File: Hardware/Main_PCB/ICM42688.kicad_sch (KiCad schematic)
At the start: 6 parts, among them U1 ICM-42688-P

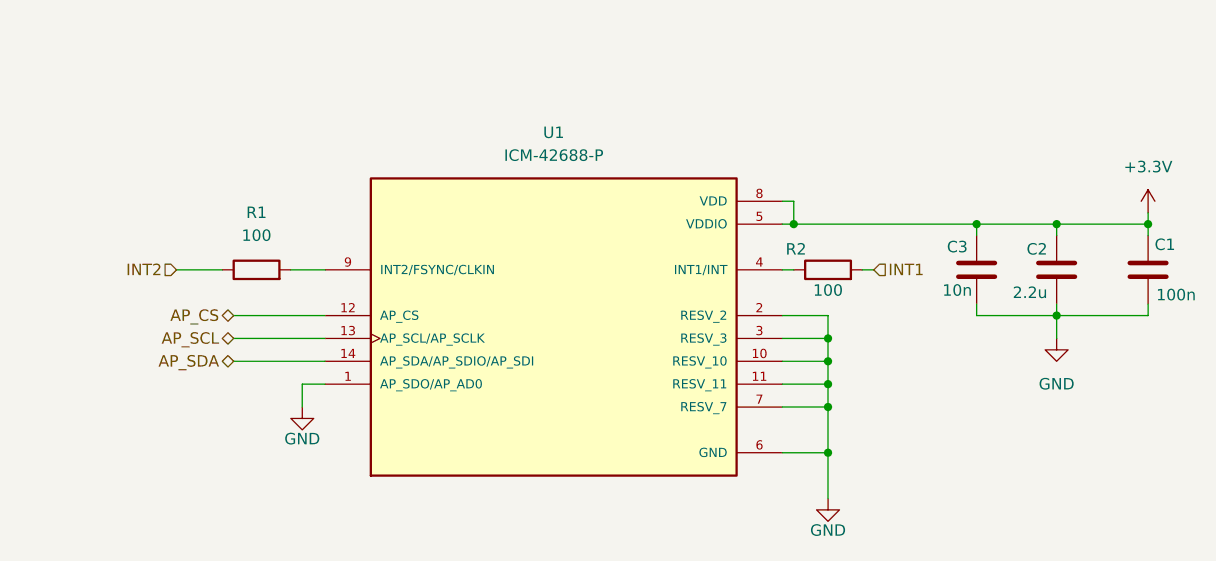
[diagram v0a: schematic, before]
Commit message: A finished version of the Main PCB schematic
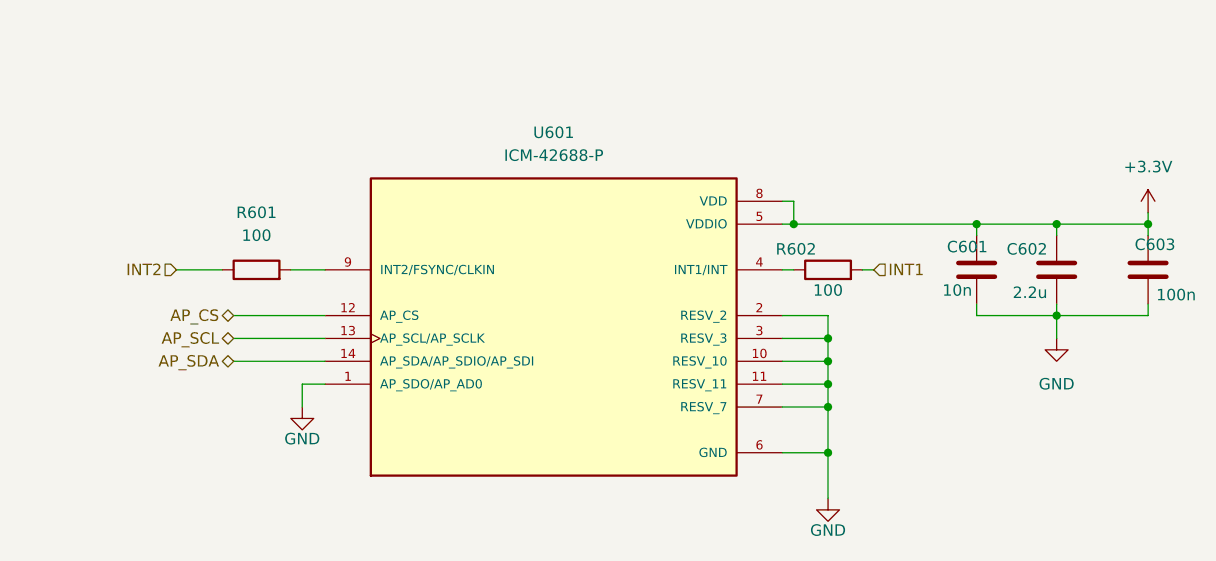
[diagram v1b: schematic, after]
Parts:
- renumbered C3 to C601, C2 to C602, C1 to C603, R1 to R601, R2 to R602, U1 to U601
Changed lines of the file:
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@@
 		(on_board yes)
 		(dnp no)
-		(property "Reference" "C3"
+		(property "Reference" "C601"
 			(at 136.398 54.61 0)
 			(effects
@@
 			(project "Main_PCB"
 				(path "/90d7beec-e1a2-46f8-bbb2-6b8f3489db10/c6d47e36-3031-4d07-ba70-df8c4b187df5"
-					(reference "C3")
+					(reference "C601")
 					(unit 1)
 				)
@@
 		(dnp no)
 		(fields_autoplaced yes)
-		(property "Reference" "R1"
+		(property "Reference" "R601"
 			(at 59.69 50.8 90)
 			(effects
@@
 			(project "Main_PCB"
 				(path "/90d7beec-e1a2-46f8-bbb2-6b8f3489db10/c6d47e36-3031-4d07-ba70-df8c4b187df5"
-					(reference "R1")
+					(reference "R601")
 					(unit 1)
 				)
@@
 		(on_board yes)
 		(dnp no)
-		(property "Reference" "C2"
+		(property "Reference" "C602"
 			(at 147.574 54.864 0)
 			(effects
@@
 			(project "Main_PCB"
 				(path "/90d7beec-e1a2-46f8-bbb2-6b8f3489db10/c6d47e36-3031-4d07-ba70-df8c4b187df5"
-					(reference "C2")
+					(reference "C602")
 					(unit 1)
 				)
@@
 		(on_board yes)
 		(dnp no)
-		(property "Reference" "R2"
+		(property "Reference" "R602"
 			(at 119.634 54.864 90)
 			(effects
@@
 			(project "Main_PCB"
 				(path "/90d7beec-e1a2-46f8-bbb2-6b8f3489db10/c6d47e36-3031-4d07-ba70-df8c4b187df5"
-					(reference "R2")
+					(reference "R602")
 					(unit 1)
 				)
@@
 		(dnp no)
 		(fields_autoplaced yes)
-		(property "Reference" "U1"
+		(property "Reference" "U601"
 			(at 92.71 41.91 0)
 			(effects
@@
 			(project "Main_PCB"
 				(path "/90d7beec-e1a2-46f8-bbb2-6b8f3489db10/c6d47e36-3031-4d07-ba70-df8c4b187df5"
-					(reference "U1")
+					(reference "U601")
 					(unit 1)
 				)
@@
 		(on_board yes)
 		(dnp no)
-		(property "Reference" "C1"
+		(property "Reference" "C603"
 			(at 161.798 54.356 0)
 			(effects
@@
 			(project "Main_PCB"
 				(path "/90d7beec-e1a2-46f8-bbb2-6b8f3489db10/c6d47e36-3031-4d07-ba70-df8c4b187df5"
-					(reference "C1")
+					(reference "C603")
 					(unit 1)
 				)
@@
 		(dnp no)
 		(fields_autoplaced yes)
-		(property "Reference" "#PWR019"
+		(property "Reference" "#PWR0604"
 			(at 158.75 54.61 0)
 			(effects
@@
 			(project "Main_PCB"
 				(path "/90d7beec-e1a2-46f8-bbb2-6b8f3489db10/c6d47e36-3031-4d07-ba70-df8c4b187df5"
-					(reference "#PWR019")
+					(reference "#PWR0604")
 					(unit 1)
 				)
@@
 		(on_board yes)
 		(dnp no)
-		(property "Reference" "#PWR022"
+		(property "Reference" "#PWR0601"
 			(at 64.77 78.74 0)
 			(effects
@@
 			(project "Main_PCB"
 				(path "/90d7beec-e1a2-46f8-bbb2-6b8f3489db10/c6d47e36-3031-4d07-ba70-df8c4b187df5"
-					(reference "#PWR022")
+					(reference "#PWR0601")
 					(unit 1)
 				)
@@
 		(on_board yes)
 		(dnp no)
-		(property "Reference" "#PWR024"
+		(property "Reference" "#PWR0602"
 			(at 123.19 88.9 0)
 			(effects
@@
 			(project "Main_PCB"
 				(path "/90d7beec-e1a2-46f8-bbb2-6b8f3489db10/c6d47e36-3031-4d07-ba70-df8c4b187df5"
-					(reference "#PWR024")
+					(reference "#PWR0602")
 					(unit 1)
 				)
@@
 		(dnp no)
 		(fields_autoplaced yes)
-		(property "Reference" "#PWR011"
+		(property "Reference" "#PWR0603"
 			(at 148.59 71.12 0)
 			(effects
@@
 			(project "Main_PCB"
 				(path "/90d7beec-e1a2-46f8-bbb2-6b8f3489db10/c6d47e36-3031-4d07-ba70-df8c4b187df5"
-					(reference "#PWR011")
-					(unit 1)
-				)
+					(reference "#PWR0603")
+					(unit 1)
+				)

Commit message: Added footprints to all components
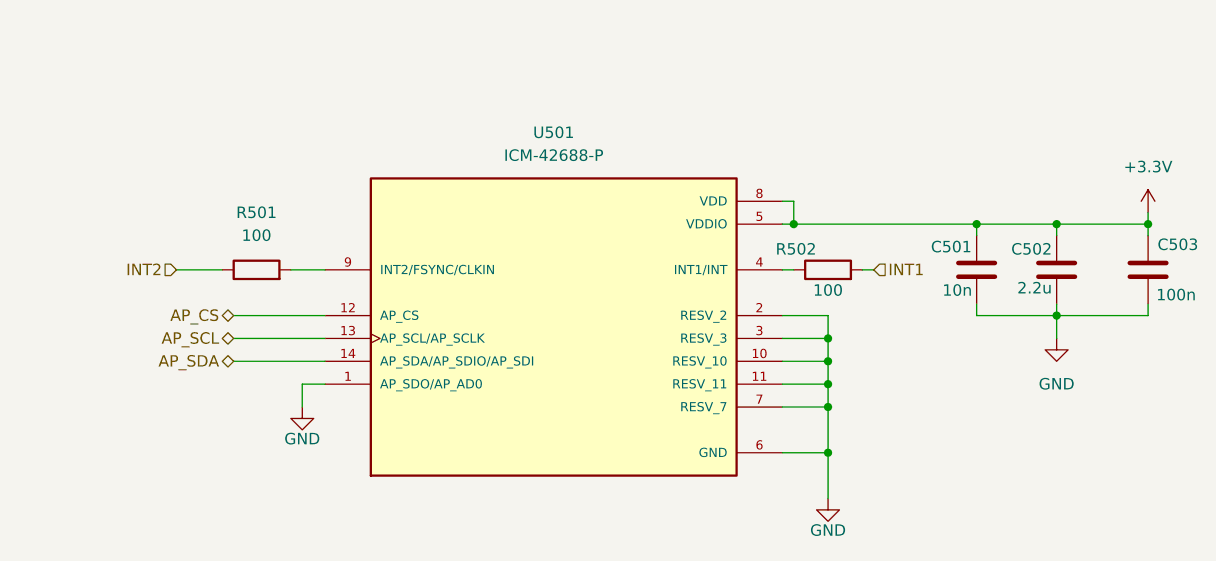
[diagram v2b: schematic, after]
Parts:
- U501: renamed from U601; footprint ICM-42688-P:PQFN50P300X250X97-14N -> MainPCB:PQFN50P300X250X97-14N
- renumbered C601 to C501, C602 to C502, C603 to C503, R601 to R501, R602 to R502
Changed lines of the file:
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@@
 		(on_board yes)
 		(dnp no)
-		(property "Reference" "C601"
-			(at 136.398 54.61 0)
+		(property "Reference" "C501"
+			(at 134.62 54.61 0)
 			(effects
 				(font
@@
 			(project "Main_PCB"
 				(path "/90d7beec-e1a2-46f8-bbb2-6b8f3489db10/c6d47e36-3031-4d07-ba70-df8c4b187df5"
-					(reference "C601")
+					(reference "C501")
 					(unit 1)
 				)
@@
 		(dnp no)
 		(fields_autoplaced yes)
-		(property "Reference" "R601"
+		(property "Reference" "R501"
 			(at 59.69 50.8 90)
 			(effects
@@
 			(project "Main_PCB"
 				(path "/90d7beec-e1a2-46f8-bbb2-6b8f3489db10/c6d47e36-3031-4d07-ba70-df8c4b187df5"
-					(reference "R601")
+					(reference "R501")
 					(unit 1)
 				)
@@
 		(on_board yes)
 		(dnp no)
-		(property "Reference" "C602"
-			(at 147.574 54.864 0)
+		(property "Reference" "C502"
+			(at 148.082 54.864 0)
 			(effects
 				(font
@@
 		)
 		(property "Value" "2.2u"
-			(at 147.574 59.69 0)
+			(at 148.082 59.182 0)
 			(effects
 				(font
@@
 			(project "Main_PCB"
 				(path "/90d7beec-e1a2-46f8-bbb2-6b8f3489db10/c6d47e36-3031-4d07-ba70-df8c4b187df5"
-					(reference "C602")
+					(reference "C502")
 					(unit 1)
 				)
@@
 		(on_board yes)
 		(dnp no)
-		(property "Reference" "R602"
+		(property "Reference" "R502"
 			(at 119.634 54.864 90)
 			(effects
@@
 			(project "Main_PCB"
 				(path "/90d7beec-e1a2-46f8-bbb2-6b8f3489db10/c6d47e36-3031-4d07-ba70-df8c4b187df5"
-					(reference "R602")
+					(reference "R502")
 					(unit 1)
 				)
@@
 		(dnp no)
 		(fields_autoplaced yes)
-		(property "Reference" "U601"
+		(property "Reference" "U501"
 			(at 92.71 41.91 0)
 			(effects
@@
 			)
 		)
-		(property "Footprint" "ICM-42688-P:PQFN50P300X250X97-14N"
+		(property "Footprint" "MainPCB:PQFN50P300X250X97-14N"
 			(at 92.71 62.23 0)
 			(effects
@@
 			(project "Main_PCB"
 				(path "/90d7beec-e1a2-46f8-bbb2-6b8f3489db10/c6d47e36-3031-4d07-ba70-df8c4b187df5"
-					(reference "U601")
+					(reference "U501")
 					(unit 1)
 				)
@@
 		(on_board yes)
 		(dnp no)
-		(property "Reference" "C603"
-			(at 161.798 54.356 0)
+		(property "Reference" "C503"
+			(at 164.338 54.356 0)
 			(effects
 				(font
@@
 			(project "Main_PCB"
 				(path "/90d7beec-e1a2-46f8-bbb2-6b8f3489db10/c6d47e36-3031-4d07-ba70-df8c4b187df5"
-					(reference "C603")
+					(reference "C503")
 					(unit 1)
 				)
@@
 		(dnp no)
 		(fields_autoplaced yes)
-		(property "Reference" "#PWR0604"
+		(property "Reference" "#PWR0504"
 			(at 158.75 54.61 0)
 			(effects
@@
 			(project "Main_PCB"
 				(path "/90d7beec-e1a2-46f8-bbb2-6b8f3489db10/c6d47e36-3031-4d07-ba70-df8c4b187df5"
-					(reference "#PWR0604")
+					(reference "#PWR0504")
 					(unit 1)
 				)
@@
 		(on_board yes)
 		(dnp no)
-		(property "Reference" "#PWR0601"
+		(property "Reference" "#PWR0501"
 			(at 64.77 78.74 0)
 			(effects
@@
 			(project "Main_PCB"
 				(path "/90d7beec-e1a2-46f8-bbb2-6b8f3489db10/c6d47e36-3031-4d07-ba70-df8c4b187df5"
-					(reference "#PWR0601")
+					(reference "#PWR0501")
 					(unit 1)
 				)
@@
 		(on_board yes)
 		(dnp no)
-		(property "Reference" "#PWR0602"
+		(property "Reference" "#PWR0502"
 			(at 123.19 88.9 0)
 			(effects
@@
 			(project "Main_PCB"
 				(path "/90d7beec-e1a2-46f8-bbb2-6b8f3489db10/c6d47e36-3031-4d07-ba70-df8c4b187df5"
-					(reference "#PWR0602")
+					(reference "#PWR0502")
 					(unit 1)
 				)
@@
 		(dnp no)
 		(fields_autoplaced yes)
-		(property "Reference" "#PWR0603"
+		(property "Reference" "#PWR0503"
 			(at 148.59 71.12 0)
 			(effects
@@
 			(project "Main_PCB"
 				(path "/90d7beec-e1a2-46f8-bbb2-6b8f3489db10/c6d47e36-3031-4d07-ba70-df8c4b187df5"
-					(reference "#PWR0603")
-					(unit 1)
-				)
+					(reference "#PWR0503")
+					(unit 1)
+				)

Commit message: Changed the IMU sensor on the MainPCB
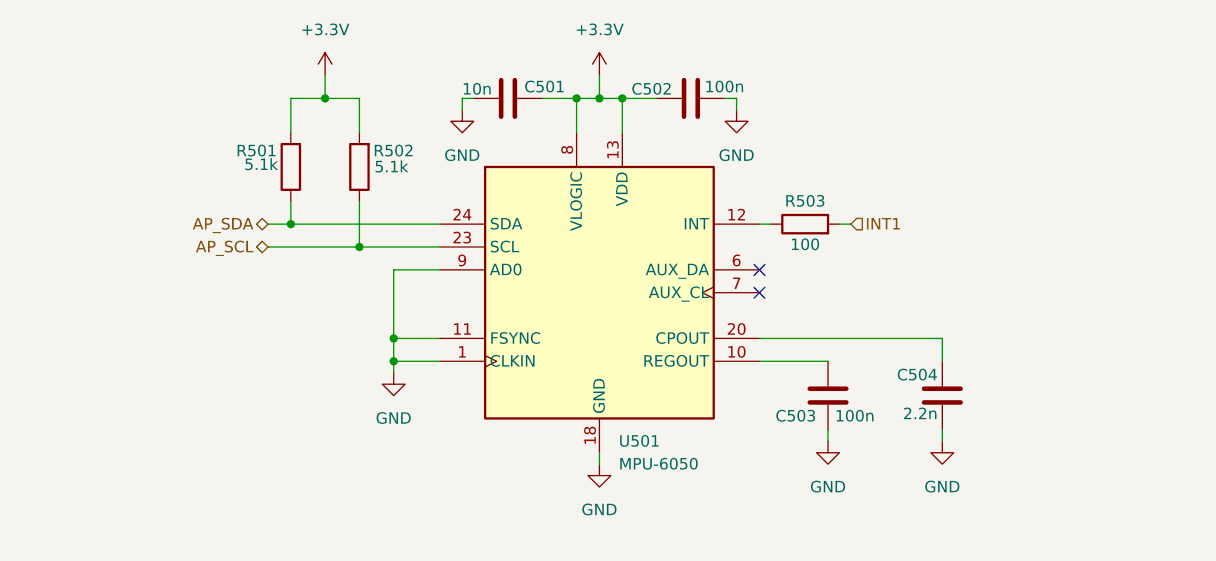
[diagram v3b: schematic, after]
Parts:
- removed C502: 2.2u, Capacitor_SMD:C_0805_2012Metric_Pad1.18x1.45mm_HandSolder, symbol Device:C
- removed U501: ICM-42688-P, MainPCB:PQFN50P300X250X97-14N, symbol ICM-42688-P:ICM-42688-P
- added C503: 100n, Capacitor_SMD:C_0603_1608Metric_Pad1.08x0.95mm_HandSolder, symbol Device:C
- added C504: 2.2n, Capacitor_SMD:C_0603_1608Metric_Pad1.08x0.95mm_HandSolder, symbol Device:C
- added R503: 100, Resistor_SMD:R_0603_1608Metric_Pad0.98x0.95mm_HandSolder, symbol Device:R
- added U501: MPU-6050, Sensor_Motion:InvenSense_QFN-24_4x4mm_P0.5mm, symbol Sensor_Motion:MPU-6050
- R501, R502: value 100 -> 5.1k
- renumbered C503 to C502
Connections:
- net INT2 is gone; now on net AP_SDA: R501.1
- net +3.3V: now also C501.2, R501.2, R502.2, U501.13 (VDD), U501.8 (VLOGIC); no longer C501.1
- net AP_SCL: now also R502.1, U501.23 (SCL)
- net AP_SDA: now also U501.24 (SDA)
- net GND: now also C501.1, C503.2, C504.1, U501.1 (CLKIN), U501.11 (FSYNC), U501.18 (GND), U501.9 (AD0); no longer C501.2
- net INT1: now also R503.2; no longer R502.2
- new net: C504.2, U501.20 (CPOUT)
- new net: C503.1, U501.10 (REGOUT)
- new net: R503.1, U501.12 (INT)
- no-connect marks 0 -> 2
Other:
- moved on the sheet: C501, C502

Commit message: Minor adjustments to MainPCB
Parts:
- C501: footprint Capacitor_SMD:C_0805_2012Metric_Pad1.18x1.45mm_HandSolder -> Capacitor_SMD:C_0603_1608Metric_Pad1.08x0.95mm_HandSolder
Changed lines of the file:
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@@
 			)
 		)
-		(property "Footprint" "Capacitor_SMD:C_0805_2012Metric_Pad1.18x1.45mm_HandSolder"
+		(property "Footprint" "Capacitor_SMD:C_0603_1608Metric_Pad1.08x0.95mm_HandSolder"
 			(at 91.44 37.1348 0)
 			(effects

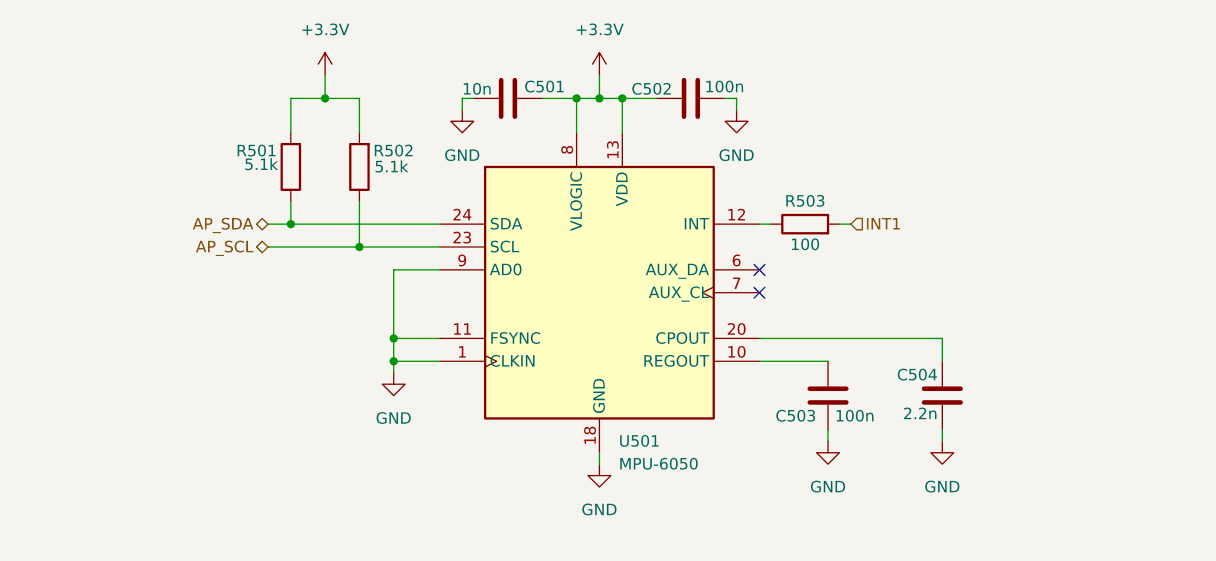
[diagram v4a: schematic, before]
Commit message: Reverted to the previous IMU
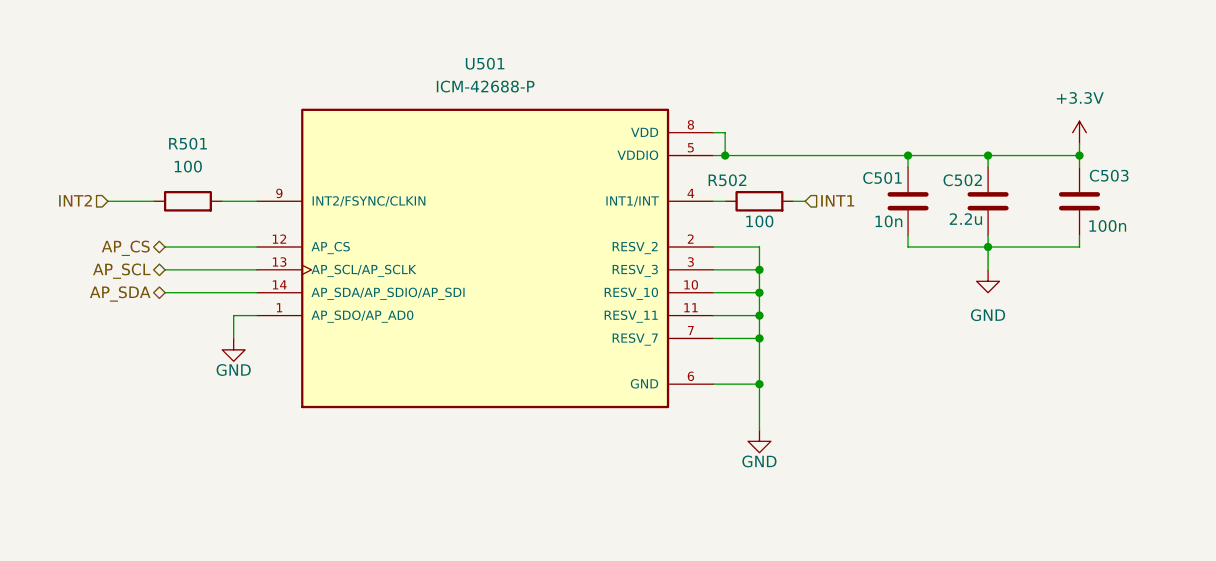
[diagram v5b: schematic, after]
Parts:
- removed C503: 100n, Capacitor_SMD:C_0603_1608Metric_Pad1.08x0.95mm_HandSolder, symbol Device:C
- removed C504: 2.2n, Capacitor_SMD:C_0603_1608Metric_Pad1.08x0.95mm_HandSolder, symbol Device:C
- removed R503: 100, Resistor_SMD:R_0603_1608Metric_Pad0.98x0.95mm_HandSolder, symbol Device:R
- removed U501: MPU-6050, Sensor_Motion:InvenSense_QFN-24_4x4mm_P0.5mm, symbol Sensor_Motion:MPU-6050
- added C502: 2.2u, Capacitor_SMD:C_0805_2012Metric_Pad1.18x1.45mm_HandSolder, symbol Device:C
- added U501: ICM-42688-P, MainPCB:PQFN50P300X250X97-14N, symbol ICM-42688-P:ICM-42688-P
- C501: footprint Capacitor_SMD:C_0603_1608Metric_Pad1.08x0.95mm_HandSolder -> Capacitor_SMD:C_0805_2012Metric_Pad1.18x1.45mm_HandSolder
- R501, R502: value 5.1k -> 100
- renumbered C502 to C503
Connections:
- net +3.3V: now also C501.1, C502.2, U501.5 (VDDIO), U501.8 (VDD); no longer C501.2, R501.2, R502.2
- net AP_SCL: now also U501.13 (AP_SCL/AP_SCLK); no longer R502.1
- net AP_SDA: now also U501.14 (AP_SDA/AP_SDIO/AP_SDI); no longer R501.1
- net GND: now also C501.2, C502.1, U501.1 (AP_SDO/AP_AD0), U501.10 (RESV_10), U501.11 (RESV_11), U501.2 (RESV_2), U501.3 (RESV_3), U501.6 (GND), U501.7 (RESV_7); no longer C501.1
- net INT1: now also R502.2
- new net: R501.2, U501.9 (INT2/FSYNC/CLKIN)
- new net: R502.1, U501.4 (INT1/INT)
- new net AP_CS: U501.12 (AP_CS)
- new net INT2: R501.1
- no-connect marks 2 -> 0
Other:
- moved on the sheet: C501, C503

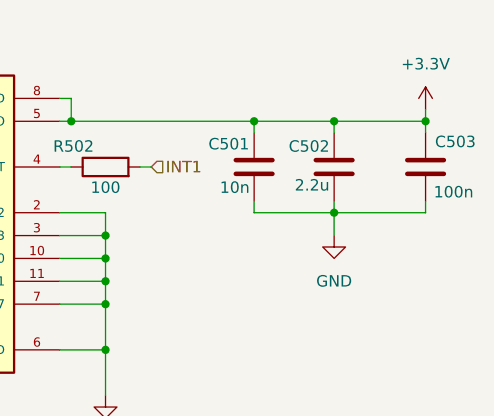
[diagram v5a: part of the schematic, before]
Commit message: Stitching GND, silkscreen thickness, increased thermal distribution of charger IC
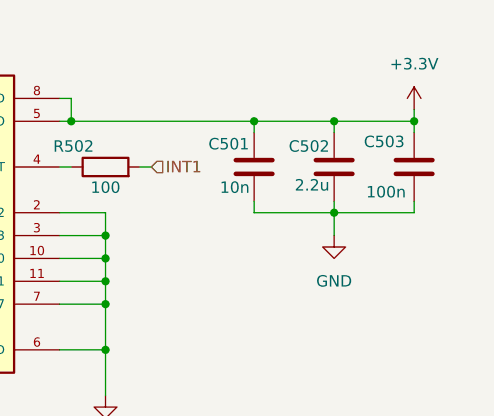
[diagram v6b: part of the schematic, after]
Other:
- moved on the sheet: C503
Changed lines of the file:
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@@
+	)
+	(junction
+		(at 149.86 44.45)
+		(diameter 0)
+		(color 0 0 0 0)
 	)
 	(junction
@@
 	)
 	(junction
-		(at 151.13 44.45)
-		(diameter 0)
-		(color 0 0 0 0)
-	)
-	(junction
 		(at 115.57 64.77)
 		(diameter 0)
@@
 	(wire
 		(pts
-			(xy 140.97 54.61) (xy 151.13 54.61)
+			(xy 140.97 54.61) (xy 149.86 54.61)
 		)
 		(stroke
@@
 	(wire
 		(pts
-			(xy 151.13 45.72) (xy 151.13 44.45)
+			(xy 149.86 45.72) (xy 149.86 44.45)
 		)
 		(stroke
@@
 	(wire
 		(pts
-			(xy 151.13 53.34) (xy 151.13 54.61)
+			(xy 149.86 53.34) (xy 149.86 54.61)
 		)
 		(stroke
@@
 	(wire
 		(pts
-			(xy 140.97 44.45) (xy 151.13 44.45)
-		)
-		(stroke
-			(width 0)
-			(type default)
-		)
-	)
-	(wire
-		(pts
-			(xy 151.13 43.18) (xy 151.13 44.45)
+			(xy 140.97 44.45) (xy 149.86 44.45)
+		)
+		(stroke
+			(width 0)
+			(type default)
+		)
+	)
+	(wire
+		(pts
+			(xy 149.86 43.18) (xy 149.86 44.45)
 		)
 		(stroke
@@
 	(symbol
 		(lib_id "Device:C")
-		(at 151.13 49.53 180)
+		(at 149.86 49.53 0)
+		(mirror x)
 		(unit 1)
 		(exclude_from_sim no)
@@
 		(dnp no)
 		(property "Reference" "C503"
-			(at 156.718 46.736 0)
+			(at 144.272 46.736 0)
 			(effects
 				(font
@@
 		)
 		(property "Value" "100n"
-			(at 156.464 52.324 0)
+			(at 144.526 52.324 0)
 			(effects
 				(font
@@
 		)
 		(property "Footprint" "Capacitor_SMD:C_0805_2012Metric_Pad1.18x1.45mm_HandSolder"
-			(at 150.1648 45.72 0)
+			(at 150.8252 45.72 0)
 			(effects
 				(font
@@
 		)
 		(property "Datasheet" "~"
-			(at 151.13 49.53 0)
+			(at 149.86 49.53 0)
 			(effects
 				(font
@@
 		)
 		(property "Description" "Unpolarized capacitor"
-			(at 151.13 49.53 0)
+			(at 149.86 49.53 0)
 			(effects
 				(font
@@
 	(symbol
 		(lib_id "power:+3.3V")
-		(at 151.13 43.18 0)
+		(at 149.86 43.18 0)
 		(unit 1)
 		(exclude_from_sim no)
@@
 		(fields_autoplaced yes)
 		(property "Reference" "#PWR0504"
-			(at 151.13 46.99 0)
+			(at 149.86 46.99 0)
 			(effects
 				(font
@@
 		)
 		(property "Value" "+3.3V"
-			(at 151.13 38.1 0)
+			(at 149.86 38.1 0)
 			(effects
 				(font
@@
 		)
 		(property "Footprint" ""
-			(at 151.13 43.18 0)
+			(at 149.86 43.18 0)
 			(effects
 				(font
@@
 		)
 		(property "Datasheet" ""
-			(at 151.13 43.18 0)
+			(at 149.86 43.18 0)
 			(effects
 				(font
@@
 		)
 		(property "Description" "Power symbol creates a global label with name \"+3.3V\""
-			(at 151.13 43.18 0)
-			(effects
-				(font
+			(at 149.86 43.18 0)
+			(effects
+				(font
